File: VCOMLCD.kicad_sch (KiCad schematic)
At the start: 35 parts, among them J3 Conn_01x05, J4 Conn_01x03, Q1 BC847, SW1 SYS_RST, SW2 BTN, U3 74LVC4245A, U4 LCD-016N002L

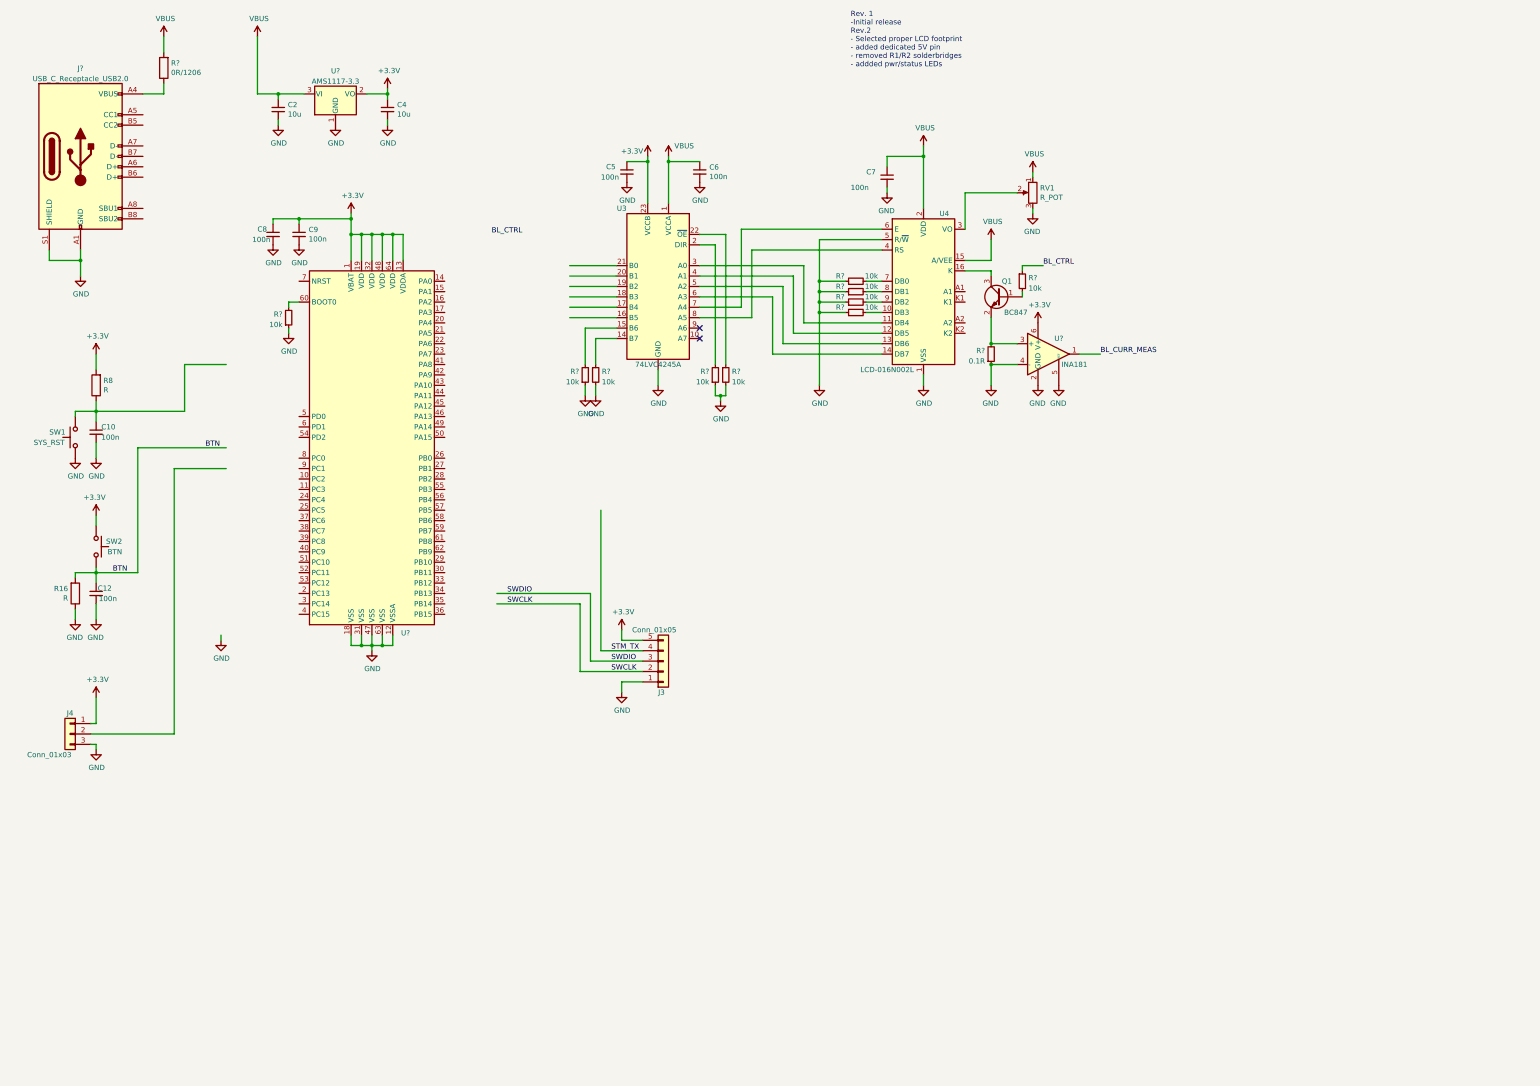
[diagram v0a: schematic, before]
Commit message: work on new STM version - basic schematic and some of pcb
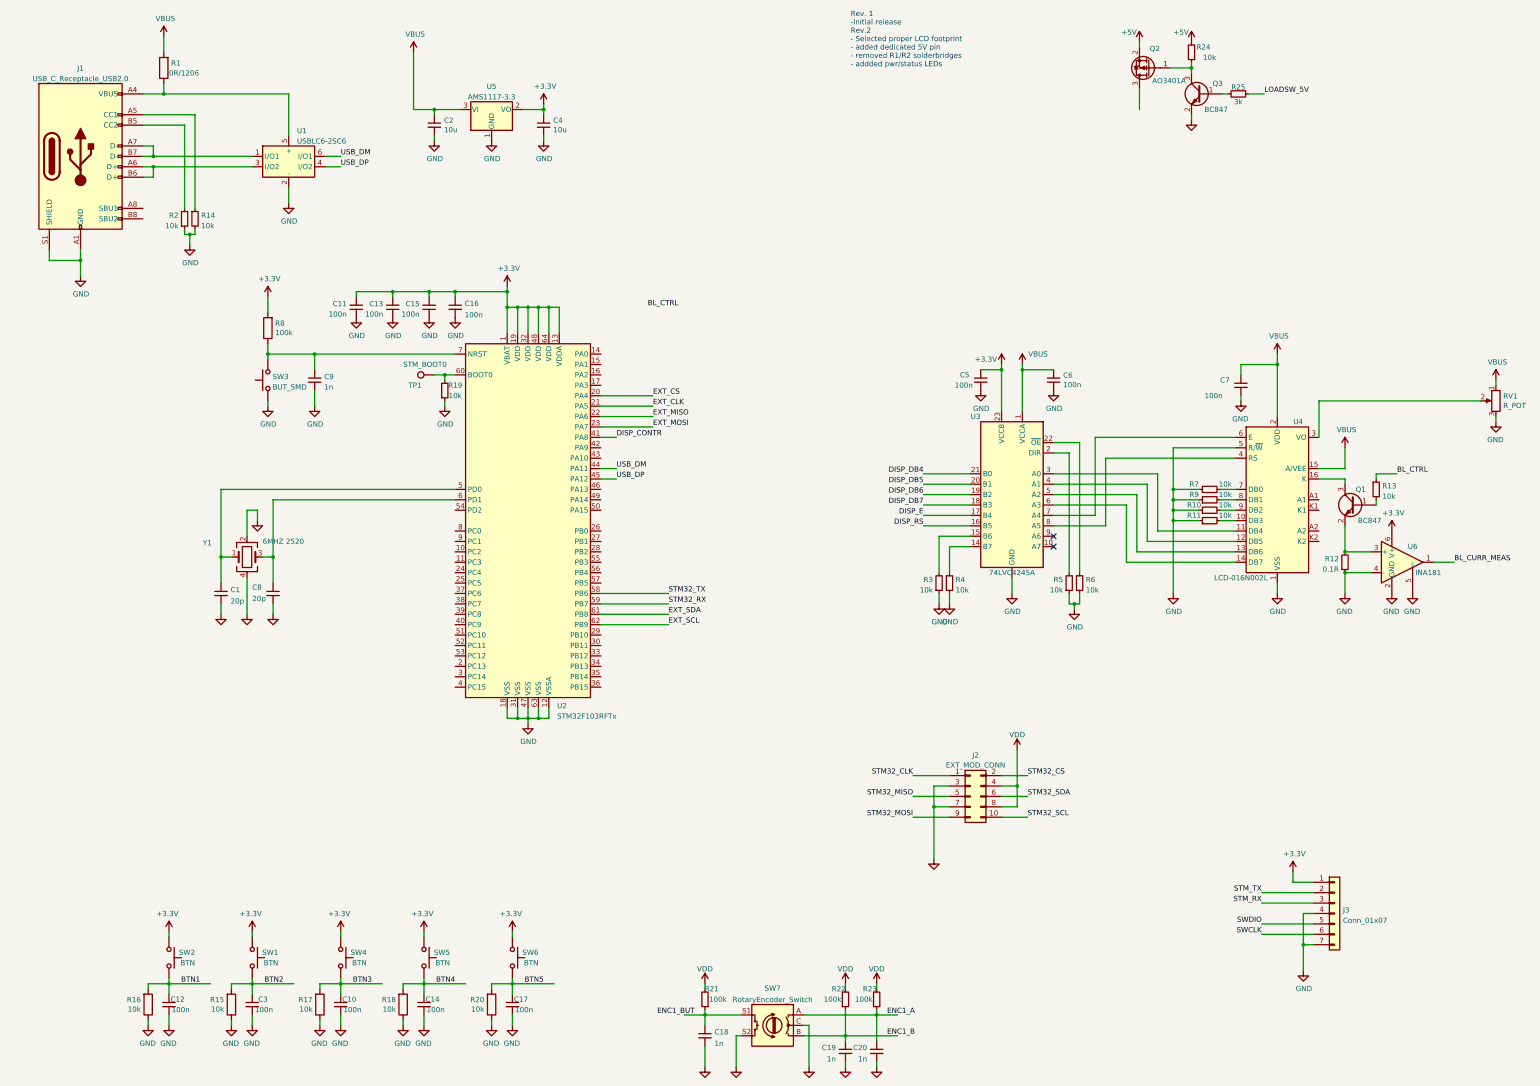
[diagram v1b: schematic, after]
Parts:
- removed J3: Conn_01x05, Connector_PinHeader_2.54mm:PinHeader_1x05_P2.54mm_Horizontal, symbol Connector_Generic:Conn_01x05
- removed J4: Conn_01x03, Connector_PinHeader_2.54mm:PinHeader_1x03_P2.54mm_Horizontal, symbol Connector_Generic:Conn_01x03
- removed R?: 10k, symbol Device:R_Small
- added C1: 20p, Capacitor_SMD:C_0402_1005Metric, symbol Device:C_Small
- added C11, C13, C14, C15, C16, C17, C3: 100n, Capacitor_SMD:C_0402_1005Metric, symbol Device:C_Small
- added C18, C19, C20: 1n, Capacitor_SMD:C_0402_1005Metric, symbol Device:C_Small
- added J2: EXT_MOD_CONN, Connector_PinSocket_2.54mm:PinSocket_2x05_P2.54mm_Vertical, symbol Connector_Generic:Conn_02x05_Odd_Even
- added J3: Conn_01x07, Connector_PinHeader_2.54mm:PinHeader_1x07_P2.54mm_Vertical, symbol Connector_Generic:Conn_01x07
- added Q2: AO3401A, Package_TO_SOT_SMD:SOT-23, symbol Transistor_FET:AO3401A
- added Q3: BC847, Package_TO_SOT_SMD:SOT-23, symbol Transistor_BJT:BC847
- added R14, R19, R2, R24: 10k, Resistor_SMD:R_0402_1005Metric, symbol Device:R_Small
- added R15, R17, R18, R20: 10k, Resistor_SMD:R_0402_1005Metric, symbol Device:R
- added R21, R22, R23: 100k, Resistor_SMD:R_0402_1005Metric, symbol Device:R_Small
- added R25: 3k, Resistor_SMD:R_0402_1005Metric, symbol Device:R_Small
- added SW3: BUT_SMD, Button_Switch_SMD:Panasonic_EVQPUM_EVQPUD, symbol Switch:SW_Push
- added SW4, SW5, SW6: BTN, Button_Switch_Keyboard:SW_Cherry_MX_1.00u_PCB, symbol Switch:SW_Push
- added SW7: RotaryEncoder_Switch, Rotary_Encoder:RotaryEncoder_Alps_EC12E-Switch_Vertical_H20mm_CircularMountingHoles, symbol Device:RotaryEncoder_Switch
- added TP1: STM_BOOT0, TestPoint:TestPoint_Pad_D1.0mm, symbol Connector:TestPoint
- added U1: USBLC6-2SC6, Package_TO_SOT_SMD:SOT-23-6, symbol Critbit_lib:USBLC6-2SC6
- added Y1: 6MHZ 2520, Crystal:Crystal_SMD_2520-4Pin_2.5x2.0mm, symbol Device:Crystal_GND24
- C10, C12, C5, C6, C7: footprint Capacitor_SMD:C_0603_1608Metric_Pad1.05x0.95mm_HandSolder -> Capacitor_SMD:C_0402_1005Metric
- C2, C4: footprint Capacitor_SMD:C_1206_3216Metric_Pad1.42x1.75mm_HandSolder -> Capacitor_SMD:C_0402_1005Metric
- C8: value 100n -> 20p; footprint Capacitor_SMD:C_0603_1608Metric_Pad1.05x0.95mm_HandSolder -> Capacitor_SMD:C_0402_1005Metric
- C9: value 100n -> 1n; footprint Capacitor_SMD:C_0603_1608Metric_Pad1.05x0.95mm_HandSolder -> Capacitor_SMD:C_0402_1005Metric
- J1: renamed from J?; footprint (none) -> Connector_USB:USB_C_Receptacle_GCT_USB4085
- R1: renamed from R?; footprint Resistor_SMD:R_0603_1608Metric_Pad1.05x0.95mm_HandSolder -> Resistor_SMD:R_1206_3216Metric_Pad1.30x1.75mm_HandSolder
- R10, R11, R13, R3, R4, R5, R6, R7, R9: renamed from R?; footprint (none) -> Resistor_SMD:R_0402_1005Metric
- R12: renamed from R?; footprint (none) -> Resistor_SMD:R_1206_3216Metric_Pad1.30x1.75mm_HandSolder
- R16: value R -> 10k; footprint Resistor_SMD:R_0603_1608Metric_Pad1.05x0.95mm_HandSolder -> Resistor_SMD:R_0402_1005Metric
- R8: value R -> 100k; footprint Resistor_SMD:R_0603_1608Metric_Pad1.05x0.95mm_HandSolder -> Resistor_SMD:R_0402_1005Metric
- SW1: value SYS_RST -> BTN; footprint Button_Switch_THT:SW_Tactile_SPST_Angled_PTS645Vx83-2LFS -> Button_Switch_Keyboard:SW_Cherry_MX_1.00u_PCB
- SW2: footprint Button_Switch_THT:SW_Tactile_SPST_Angled_PTS645Vx83-2LFS -> Button_Switch_Keyboard:SW_Cherry_MX_1.00u_PCB
- U2: renamed from U?; value (none) -> STM32F103RFTx; footprint (none) -> Package_QFP:LQFP-64_10x10mm_P0.5mm
- gave numbers to parts that had none: 2
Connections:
- net +3V3: now also SW1.2, C11.2, C13.2, C15.2, C16.1, J3.1 (Pin_1), SW4.2, SW5.2, SW6.2; no longer C8.1, C9.1
- net GND: now also C1.2, C11.1, C13.1, C14.2, C15.1, C16.2, C17.2, C18.2, C19.2, C20.2, C3.2, J2.3 (Pin_3), J2.7 (Pin_7), J3.4 (Pin_4), J3.7 (Pin_7), Q3.2 (E), R14.2, R15.1, R17.1, R18.1, R19.1, R2.1, R20.1, SW3.1, SW7.C, SW7.S2, U1.2 (-), Y1.2, Y1.4; no longer SW1.1
- net STM_TX: now also J3.2 (Pin_2)
- net SWCLK: now also J3.6 (Pin_6)
- net SWDIO: now also J3.5 (Pin_5)
- net DISP_RS: now reaches U3.16 (B5)
- net DISP_E: now reaches U3.17 (B4)
- net DISP_DB7: now reaches U3.18 (B3)
- net DISP_DB6: now reaches U3.19 (B2)
- net DISP_DB5: now reaches U3.20 (B1)
- net DISP_DB4: now reaches U3.21 (B0)
- net at J1.A4 (VBUS), J1.A9 (VBUS), J1.B4 (VBUS)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: now also U1.5 (+)
- net at J1.A5 (CC1): now also R14.1
- net at J1.A6 (D+): now also J1.B6 (D+), U1.3 (I/O2)
- net at J1.A7 (D-): now also J1.B7 (D-), U1.1 (I/O1)
- net at J1.B5 (CC2): now also R2.2
- net EXT_CS: now reaches U2.20 (PA4)
- net EXT_CLK: now reaches U2.21 (PA5)
- net EXT_MISO: now reaches U2.22 (PA6)
- net EXT_MOSI: now reaches U2.23 (PA7)
- net DISP_CONTR: now reaches U2.41 (PA8)
- net USB_DM: now reaches U2.44 (PA11)
- net USB_DM: now also U1.6 (I/O1)
- net USB_DP: now reaches U2.45 (PA12)
- net USB_DP: now also U1.4 (I/O2)
- net at U2.5 (PD0): now also C1.1, Y1.1
- net STM32_TX: now reaches U2.58 (PB6)
- net STM32_RX: now reaches U2.59 (PB7)
- net at U2.6 (PD1): now also C8.1, Y1.3
- net at U2.60 (BOOT0): now also R19.2, TP1.1
- net EXT_SDA: now reaches U2.61 (PB8)
- net EXT_SCL: now reaches U2.62 (PB9)
- net at U2.7 (NRST): now also C9.1, R8.1, SW3.2
- net BTN renamed BTN1
- new net: Q2.1 (G), Q3.3 (C), R24.1
- new net: Q3.1 (B), R25.2
- new net +5V: Q2.2 (S), R24.2
- new net BTN2: C3.1, R15.2, SW1.1
- new net BTN3: C10.1, R17.2, SW4.1
- new net BTN4: C14.1, R18.2, SW5.1
- new net BTN5: C17.1, R20.2, SW6.1
- new net ENC1_A: C20.1, R23.1, SW7.A
- new net ENC1_B: C19.1, R22.1, SW7.B
- new net ENC1_BUT: C18.1, R21.1, SW7.S1
- new net LOADSW_5V: R25.1
- new net STM32_CLK: J2.1 (Pin_1)
- new net STM32_CS: J2.2 (Pin_2)
- new net STM32_MISO: J2.5 (Pin_5)
- new net STM32_MOSI: J2.9 (Pin_9)
- new net STM32_SCL: J2.10 (Pin_10)
- new net STM32_SDA: J2.6 (Pin_6)
- new net STM_RX: J3.3 (Pin_3)
- new net VDD: J2.4 (Pin_4), J2.8 (Pin_8), R21.2, R22.2, R23.2
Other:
- moved on the sheet: C12, C2, C4, C5, C6, C7, Q1, R10, R11, R12, R13, R16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

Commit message: WIP commit
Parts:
- removed J2: EXT_MOD_CONN, Connector_PinSocket_2.54mm:PinSocket_2x05_P2.54mm_Vertical, symbol Connector_Generic:Conn_02x05_Odd_Even
- removed Q2: AO3401A, Package_TO_SOT_SMD:SOT-23, symbol Transistor_FET:AO3401A
- removed Q3: BC847, Package_TO_SOT_SMD:SOT-23, symbol Transistor_BJT:BC847
- removed R24: 10k, Resistor_SMD:R_0402_1005Metric, symbol Device:R_Small
- removed R25: 3k, Resistor_SMD:R_0402_1005Metric, symbol Device:R_Small
- added J? (x2): Conn_01x08, symbol Connector_Generic:Conn_01x08
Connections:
- net GND: now also J?.7 (Pin_7)
- net VBUS: now also J?.8 (Pin_8)
- net VDD: now also J?.8 (Pin_8)
- net EXT_CLK renamed MOD1_SCLK
- net MOD1_SCLK: now also J?.4 (Pin_4)
- net EXT_CS renamed MOD1_CS
- net MOD1_CS: now also J?.7 (Pin_7)
- net EXT_MISO renamed MOD1_MISO
- net MOD1_MISO: now also J?.5 (Pin_5)
- net EXT_MOSI renamed MOD1_MOSI
- net MOD1_MOSI: now also J?.6 (Pin_6)
- net EXT_SCL renamed MODx_SCL
- net MODx_SCL: now also J?.3 (Pin_3)
- net EXT_SDA renamed MODx_SDA
- net MODx_SDA: now also J?.4 (Pin_4)
- new net MOD1_RXD: J?.1 (Pin_1)
- new net MOD1_TXD: J?.2 (Pin_2)
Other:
- note added: "MOD_RST MOD_ANA MOD_ISR MOD_SCLK MOD_MISO MOD_MOSI MOD_CS MOD_3V3"
- note added: "MOD_TXD MOD_RXD MOD_SCL MOD_SDA MOD_IO1 MOD_IO2 MOD_GND MOD_5V"
- moved on the sheet: C10, C12, C14, C17, C18, C19, C20, C3, C5, C6, C7, J3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
